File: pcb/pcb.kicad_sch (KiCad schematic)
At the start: 0 parts

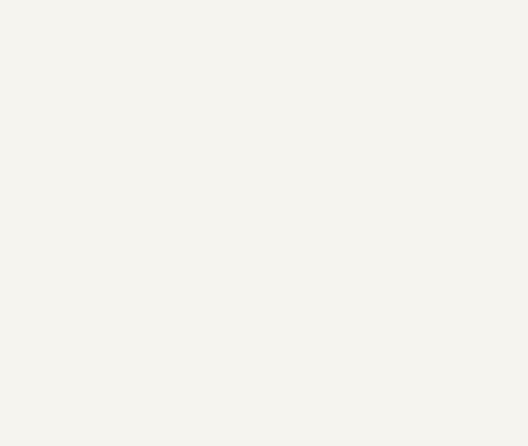
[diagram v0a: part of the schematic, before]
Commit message: add mcu sheet with finished debug connector
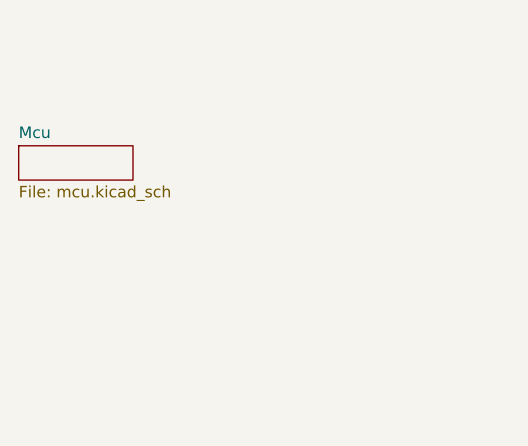
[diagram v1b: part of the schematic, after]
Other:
- added sheet Mcu (mcu.kicad_sch)
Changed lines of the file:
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@@
 (kicad_sch (version 20211123) (generator eeschema)
   (paper "A4")
+  (sheet (at 50.8 67.31) (size 12.7 3.81) (fields_autoplaced)
+    (stroke (width 0.1524) (type solid) (color 0 0 0 0))
+    (fill (color 0 0 0 0.0000))
+    (property "Sheet name" "Mcu" (id 0) (at 50.8 66.5984 0)
+      (effects (font (size 1.27 1.27)) (justify left bottom))
+    )
+    (property "Sheet file" "mcu.kicad_sch" (id 1) (at 50.8 71.7046 0)
+      (effects (font (size 1.27 1.27)) (justify left top))
+    )
+  )
   (sheet (at 187.96 55.88) (size 67.31 41.91) (fields_autoplaced)
     (stroke (width 0.1524) (type solid) (color 0 0 0 0))
@@
     (path "/" (page "1"))
     (path "/3b22a2f7-b29a-4d17-ab95-ad9be8231bab" (page "2"))
+    (path "/2aa537c7-efb0-46e2-81ad-fe9eeab0e71a" (page "3"))
   )
   (symbol_instances
     (path "/3b22a2f7-b29a-4d17-ab95-ad9be8231bab/6a054e2c-9b61-4bed-bb95-4932ecc64fa8"
+      (reference "#PWR?") (unit 1) (value "GND") (footprint "")
+    )
+    (path "/2aa537c7-efb0-46e2-81ad-fe9eeab0e71a/82540ebe-ae45-4a3b-b014-5475e7748ef9"
+      (reference "#PWR?") (unit 1) (value "VCC") (footprint "")
+    )
+    (path "/2aa537c7-efb0-46e2-81ad-fe9eeab0e71a/8fad61f1-caec-4bd2-8a47-154405c74a01"
       (reference "#PWR?") (unit 1) (value "GND") (footprint "")
     )
@@
       (reference "C?") (unit 1) (value "C") (footprint "")
     )
+    (path "/2aa537c7-efb0-46e2-81ad-fe9eeab0e71a/e52181f5-4ebd-4390-9f3e-8b706699623c"
+      (reference "J?") (unit 1) (value "mcu_debug") (footprint "")
+    )
     (path "/3b22a2f7-b29a-4d17-ab95-ad9be8231bab/0a1f7319-eb04-45b9-bba9-aeb36a6e7048"
       (reference "L?") (unit 1) (value "INDUCTOR") (footprint "")
@@
       (reference "U?") (unit 1) (value "TPS54325PWPR") (footprint "PWP14_2P31X2P46")
     )
+    (path "/2aa537c7-efb0-46e2-81ad-fe9eeab0e71a/b46b5297-888f-43e6-926a-ebe8736d3108"
+      (reference "U?") (unit 1) (value "EFM32GG990F1024") (footprint "BGA112")
+    )
+    (path "/2aa537c7-efb0-46e2-81ad-fe9eeab0e71a/59d85119-1b53-4847-86a0-a45d6daac7e6"
+      (reference "U?") (unit 2) (value "EFM32GG990F1024") (footprint "BGA112")
+    )
   )

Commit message: oops I think I updated these
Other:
- added sheet fpga (fpga.kicad_sch)

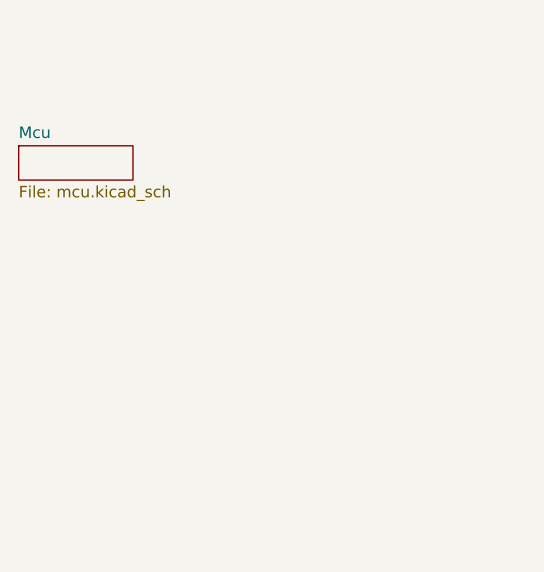
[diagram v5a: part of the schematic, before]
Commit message: added new_vga and sram
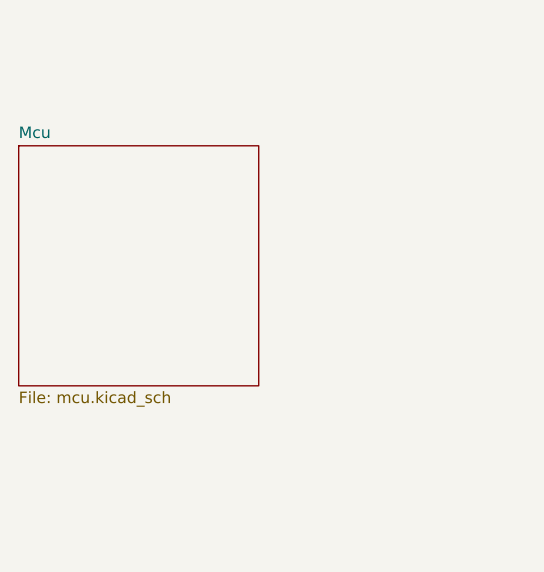
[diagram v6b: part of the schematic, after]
